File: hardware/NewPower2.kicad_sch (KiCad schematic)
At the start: 46 parts, among them SW1 K2-1156SP-F5SW-05, U2 AXP192, U3 SGM6603-ADJYN6G, U5 SGM3204

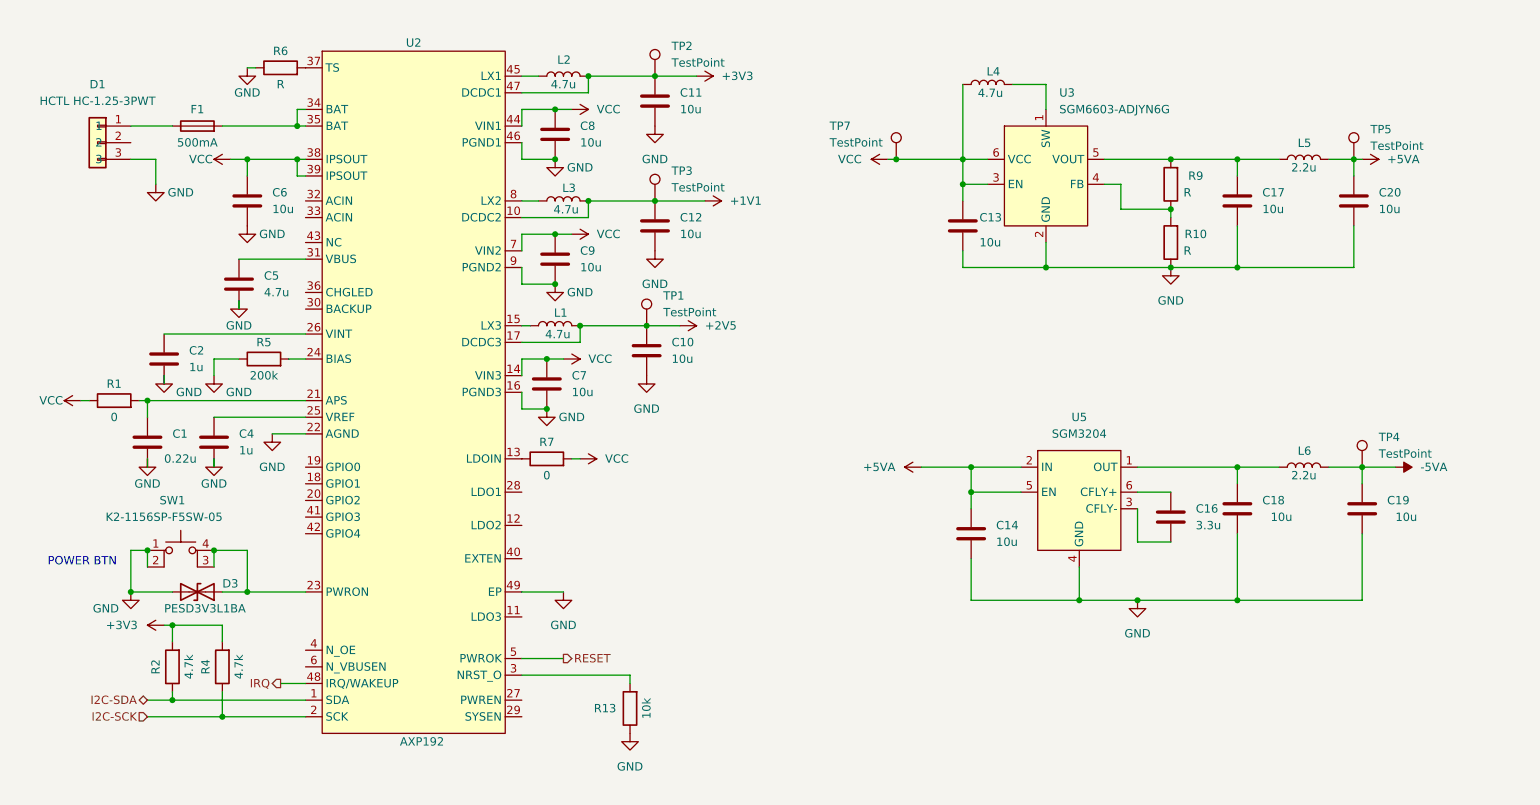
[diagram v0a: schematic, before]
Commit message: new power list added
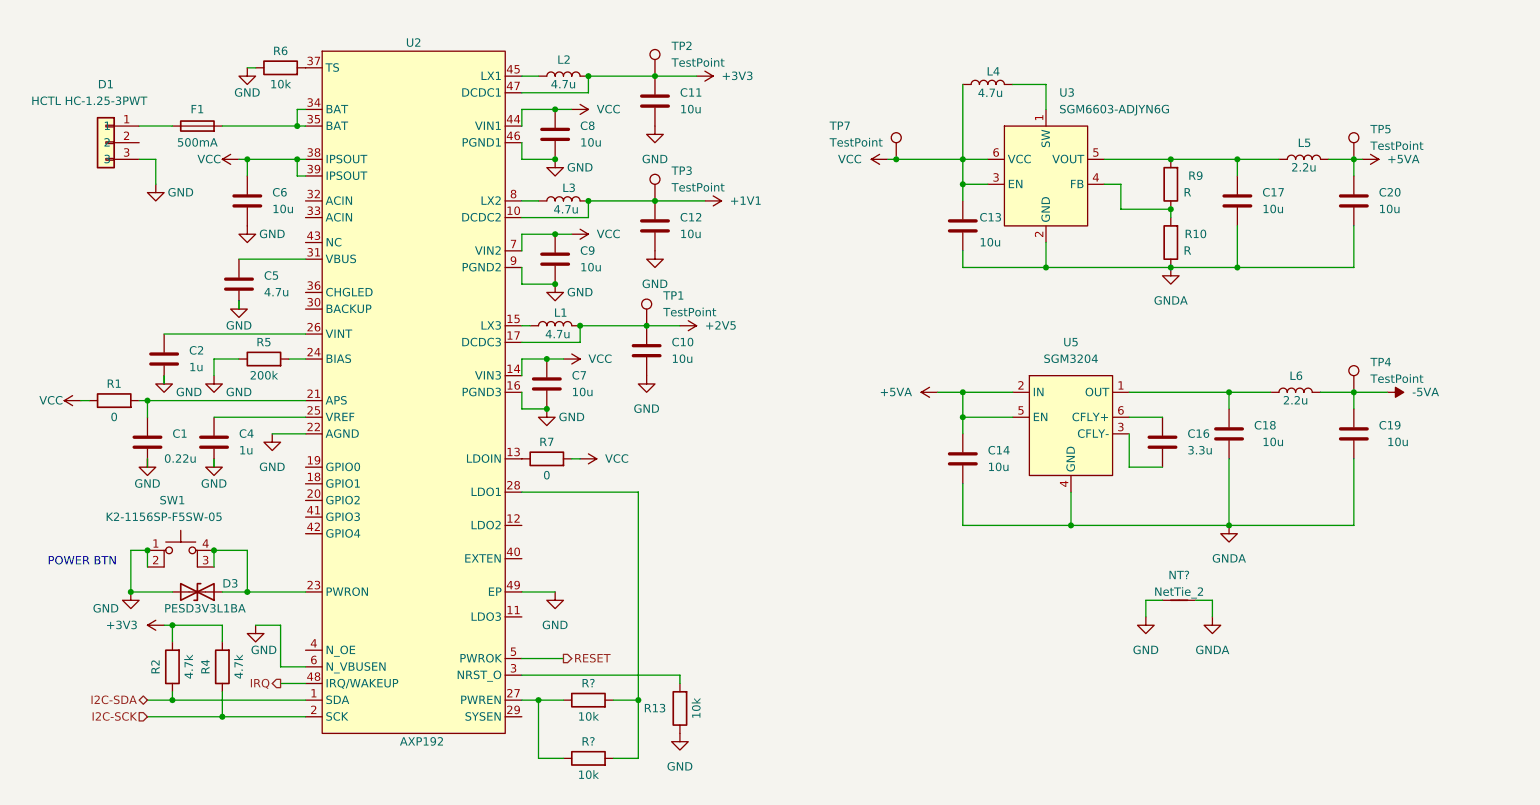
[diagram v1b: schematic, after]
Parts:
- added NT?: NetTie_2, symbol Device:NetTie_2
- added R? (x2): 10k, symbol Device:R
- L2: Mfr.  partnumber (none) -> LQH32PN4R7NN0L
- R6: value R -> 10k
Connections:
- net GND: now also U2.6 (N_VBUSEN), NT?.1; no longer C13.2, C14.2, C17.2, C18.2, C19.2, C20.2, R10.1, U3.2 (GND), U5.4 (GND)
- net at U2.27 (PWREN): now also R?.1, R?.1
- net at U2.28 (LDO1): now also R?.2, R?.2
- new net GNDA: C13.2, C14.2, C17.2, C18.2, C19.2, C20.2, NT?.2, R10.1, U3.2 (GND), U5.4 (GND)
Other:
- moved on the sheet: C14, C16, C18, C19, D1, L6, R13, TP4, U5

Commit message: some chnages
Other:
- moved on the sheet: C13, C14, C16, C17, C18, C19, C20, L4, L5, L6, NT?, R10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
